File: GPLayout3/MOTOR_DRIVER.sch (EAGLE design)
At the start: 94 parts, among them T1 2N2222, T2 2N2222, U7 ATMEGA328P_TQFP, Y1 16MHz

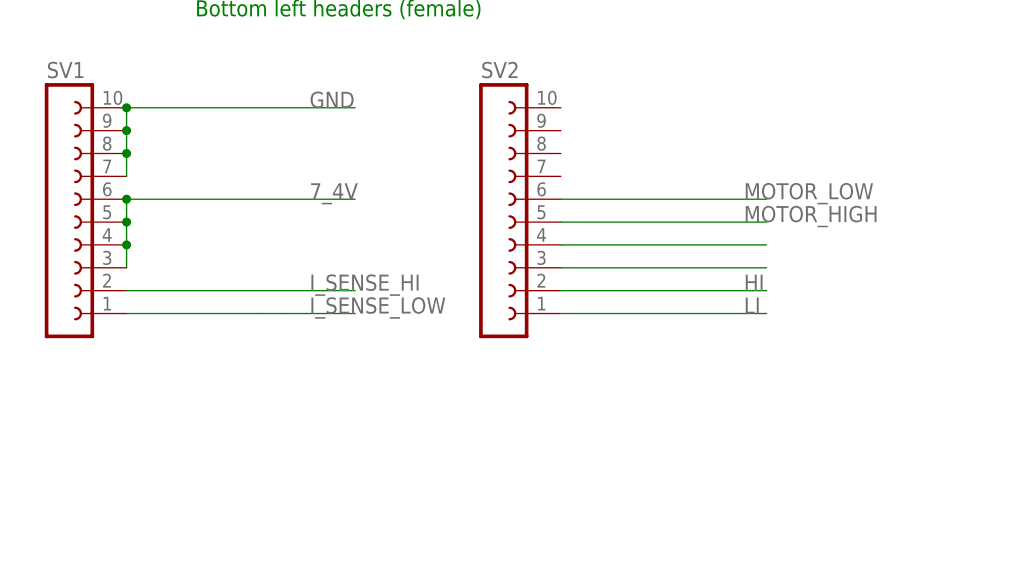
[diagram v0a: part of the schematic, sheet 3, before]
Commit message: Routed lower board and combined all boards
typical_4pcb.dru lists design errors for the width of the traces, but
the file is outdated and trace widths correspond with 4pcb's website
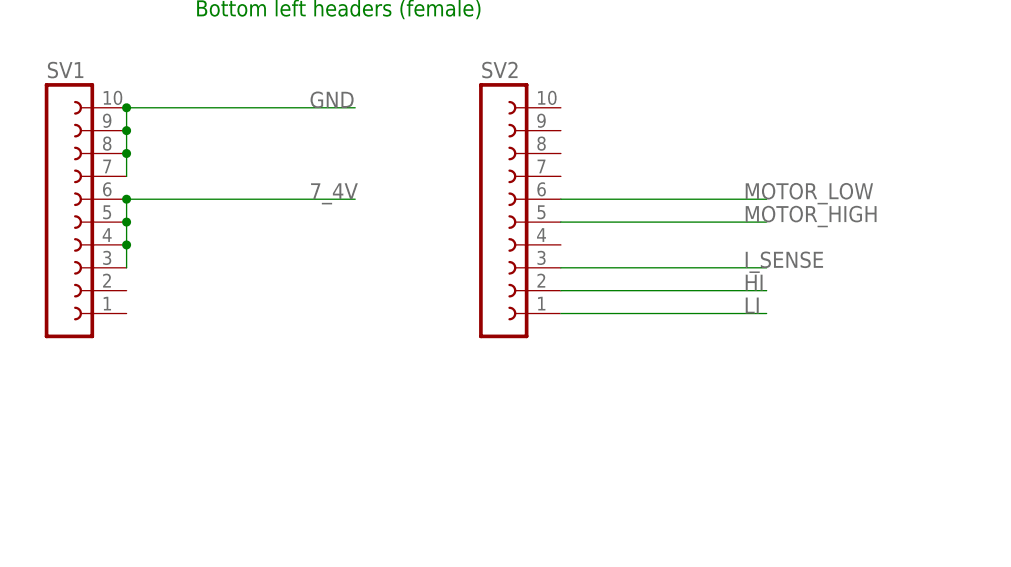
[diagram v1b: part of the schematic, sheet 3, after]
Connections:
- removed net I_SENSE_HI: SV1.2
- removed net I_SENSE_LOW: SV1.1
- net HI2: no longer SV2.3
- net I_SENSE: now also SV2.3
- net LI2: no longer SV2.4
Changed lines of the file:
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@@
 </variantdefs>
 <classes>
-<class number="0" name="default" width="0" drill="0">
-<clearance class="0" value="0.205"/>
+<class number="0" name="default" width="0.2" drill="0.6">
+<clearance class="0" value="0.2"/>
 </class>
 </classes>
@@
 </segment>
 </net>
-<net name="LI2" class="0">
-<segment>
-<pinref part="SV2" gate="G$1" pin="4"/>
-<wire x1="104.14" y1="142.24" x2="127" y2="142.24" width="0.1524" layer="91"/>
-</segment>
-</net>
-<net name="HI2" class="0">
-<segment>
-<pinref part="SV2" gate="G$1" pin="3"/>
-<wire x1="104.14" y1="139.7" x2="127" y2="139.7" width="0.1524" layer="91"/>
-</segment>
-</net>
 <net name="I_SENSE_LOW_TOP" class="0">
 <segment>
@@
 </segment>
 </net>
-<net name="I_SENSE_HI" class="0">
-<segment>
-<pinref part="SV1" gate="G$1" pin="2"/>
-<wire x1="55.88" y1="137.16" x2="81.28" y2="137.16" width="0.1524" layer="91"/>
-<label x="76.2" y="137.16" size="1.778" layer="95"/>
-</segment>
-</net>
-<net name="I_SENSE_LOW" class="0">
-<segment>
-<pinref part="SV1" gate="G$1" pin="1"/>
-<wire x1="55.88" y1="134.62" x2="71.12" y2="134.62" width="0.1524" layer="91"/>
-<wire x1="73.66" y1="134.62" x2="81.28" y2="134.62" width="0.1524" layer="91"/>
-<wire x1="73.66" y1="134.62" x2="71.12" y2="134.62" width="0.1524" layer="91"/>
-<label x="76.2" y="134.62" size="1.778" layer="95"/>
-</segment>
-</net>
 <net name="I_SENSE_TOP" class="0">
 <segment>
@@
 </segment>
 </net>
+<net name="I_SENSE" class="0">
+<segment>
+<pinref part="SV2" gate="G$1" pin="3"/>
+<wire x1="104.14" y1="139.7" x2="127" y2="139.7" width="0.1524" layer="91"/>
+<label x="124.46" y="139.7" size="1.778" layer="95"/>
+</segment>
+</net>

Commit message: added several resistor values
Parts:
- R10, R11, R9: value (none) -> 59
- R5, R7: value (none) -> 1
- renumbered SV10 to TGPIO
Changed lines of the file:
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@@
 <?xml version="1.0" encoding="utf-8"?>
 <!DOCTYPE eagle SYSTEM "eagle.dtd">
-<eagle version="8.0.0">
+<eagle version="8.0.1">
 <drawing>
 <settings>
@@
 <part name="LED_DRIVER2" library="CSD18502KCS" deviceset="CSD18502KCS_KCS_3" device=""/>
 <part name="U$7" library="ledpot" deviceset="POT" device=""/>
-<part name="R5" library="rcl" deviceset="R-US_" device="R2512"/>
+<part name="R5" library="rcl" deviceset="R-US_" device="R2512" value="1"/>
 <part name="T1" library="transistor" deviceset="2N2222" device=""/>
 <part name="R6" library="SparkFun-Resistors" deviceset="1KOHM" device="-HORIZ-1/4W-1%" value="1k"/>
 <part name="LED_DRIVER1" library="CSD18502KCS" deviceset="CSD18502KCS_KCS_3" device=""/>
 <part name="U$3" library="ledpot" deviceset="POT" device=""/>
-<part name="R7" library="rcl" deviceset="R-US_" device="R2512"/>
+<part name="R7" library="rcl" deviceset="R-US_" device="R2512" value="1"/>
 <part name="T2" library="transistor" deviceset="2N2222" device=""/>
 <part name="R8" library="SparkFun-Resistors" deviceset="1KOHM" device="-HORIZ-1/4W-1%" value="1k"/>
@@
 <part name="3_3V" library="con-lsta" deviceset="FE05-1" device=""/>
 <part name="5V" library="con-lsta" deviceset="FE05-1" device=""/>
-<part name="R9" library="rcl" deviceset="R-US_" device="R0805"/>
-<part name="R10" library="rcl" deviceset="R-US_" device="R0805"/>
-<part name="R11" library="rcl" deviceset="R-US_" device="R0805"/>
+<part name="R9" library="rcl" deviceset="R-US_" device="R0805" value="59"/>
+<part name="R10" library="rcl" deviceset="R-US_" device="R0805" value="59"/>
+<part name="R11" library="rcl" deviceset="R-US_" device="R0805" value="59"/>
 <part name="D1" library="SparkFun-LED" deviceset="LED" device="0603"/>
 <part name="D2" library="SparkFun-LED" deviceset="LED" device="0603"/>
@@
 <part name="ATGPIO" library="con-lsta" deviceset="FE10-1" device=""/>
 <part name="R17" library="rcl" deviceset="R-US_" device="R2512" value="10m"/>
-<part name="SV10" library="con-lsta" deviceset="FE08-1" device=""/>
+<part name="TGPIO" library="con-lsta" deviceset="FE08-1" device=""/>
 <part name="I_SENSE_AMP" library="burr-brown" deviceset="INA138" device=""/>
 <part name="R18" library="rcl" deviceset="R-US_" device="R0603" value="10k"/>
@@
 <instance part="R15" gate="G$1" x="360.68" y="86.36" rot="R90"/>
 <instance part="ATGPIO" gate="G$1" x="162.56" y="66.04"/>
-<instance part="SV10" gate="G$1" x="121.92" y="66.04"/>
+<instance part="TGPIO" gate="G$1" x="121.92" y="66.04"/>
 <instance part="REC" gate="G$1" x="208.28" y="91.44"/>
 </instances>
@@
 <wire x1="129.54" y1="58.42" x2="147.32" y2="58.42" width="0.1524" layer="91"/>
 <label x="139.7" y="58.42" size="1.778" layer="95"/>
-<pinref part="SV10" gate="G$1" pin="1"/>
+<pinref part="TGPIO" gate="G$1" pin="1"/>
 </segment>
 </net>
@@
 <wire x1="129.54" y1="60.96" x2="147.32" y2="60.96" width="0.1524" layer="91"/>
 <label x="139.7" y="60.96" size="1.778" layer="95"/>
-<pinref part="SV10" gate="G$1" pin="2"/>
+<pinref part="TGPIO" gate="G$1" pin="2"/>
 </segment>
 </net>
@@
 <wire x1="129.54" y1="63.5" x2="147.32" y2="63.5" width="0.1524" layer="91"/>
 <label x="139.7" y="63.5" size="1.778" layer="95"/>
-<pinref part="SV10" gate="G$1" pin="3"/>
+<pinref part="TGPIO" gate="G$1" pin="3"/>
 </segment>
 </net>
@@
 <wire x1="129.54" y1="66.04" x2="147.32" y2="66.04" width="0.1524" layer="91"/>
 <label x="139.7" y="66.04" size="1.778" layer="95"/>
-<pinref part="SV10" gate="G$1" pin="4"/>
+<pinref part="TGPIO" gate="G$1" pin="4"/>
 </segment>
 </net>
@@
 <wire x1="129.54" y1="68.58" x2="147.32" y2="68.58" width="0.1524" layer="91"/>
 <label x="139.7" y="68.58" size="1.778" layer="95"/>
-<pinref part="SV10" gate="G$1" pin="5"/>
+<pinref part="TGPIO" gate="G$1" pin="5"/>
 </segment>
 </net>
@@
 <wire x1="129.54" y1="71.12" x2="147.32" y2="71.12" width="0.1524" layer="91"/>
 <label x="139.7" y="71.12" size="1.778" layer="95"/>
-<pinref part="SV10" gate="G$1" pin="6"/>
+<pinref part="TGPIO" gate="G$1" pin="6"/>
 </segment>
 </net>
@@
 <wire x1="129.54" y1="73.66" x2="147.32" y2="73.66" width="0.1524" layer="91"/>
 <label x="139.7" y="73.66" size="1.778" layer="95"/>
-<pinref part="SV10" gate="G$1" pin="7"/>
+<pinref part="TGPIO" gate="G$1" pin="7"/>
 </segment>
 </net>
@@
 <wire x1="129.54" y1="76.2" x2="147.32" y2="76.2" width="0.1524" layer="91"/>
 <label x="139.7" y="76.2" size="1.778" layer="95"/>
-<pinref part="SV10" gate="G$1" pin="8"/>
-</segment>
-</net>
+<pinref part="TGPIO" gate="G$1" pin="8"/>
+</segment>
+</net>

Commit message: made overall dimensions smaller, moved I_SENSE and added back a GPIO. made an attempt at a gerber file
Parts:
- removed TGPIO: (no value), con-lsta:FE08-1
- added SV10: (no value), con-lsta:FE09-1
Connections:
- removed net HI2: U$1.5
- new net TGPIO9: SV10.9, U$1.A22/DAC1
- net I_SENSE: now also U$1.5; no longer U$1.A22/DAC1
- net TGPIO1: now also SV10.1; no longer TGPIO.1
- net TGPIO2: now also SV10.2; no longer TGPIO.2
- net TGPIO3: now also SV10.3; no longer TGPIO.3
- net TGPIO4: now also SV10.4; no longer TGPIO.4
- net TGPIO5: now also SV10.5; no longer TGPIO.5
- net TGPIO6: now also SV10.6; no longer TGPIO.6
- net TGPIO7: now also SV10.7; no longer TGPIO.7
- net TGPIO8: now also SV10.8; no longer TGPIO.8
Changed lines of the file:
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@@
 <part name="ATGPIO" library="con-lsta" deviceset="FE10-1" device=""/>
 <part name="R17" library="rcl" deviceset="R-US_" device="R2512" value="10m"/>
-<part name="TGPIO" library="con-lsta" deviceset="FE08-1" device=""/>
 <part name="I_SENSE_AMP" library="burr-brown" deviceset="INA138" device=""/>
 <part name="R18" library="rcl" deviceset="R-US_" device="R0603" value="10k"/>
@@
 <part name="REC" library="con-lsta" deviceset="FE06-1" device=""/>
 <part name="C8" library="rcl" deviceset="C-US" device="C0805" value="10u"/>
+<part name="SV10" library="con-lsta" deviceset="FE09-1" device=""/>
 </parts>
 <sheets>
@@
 </segment>
 </net>
-<net name="HI2" class="0">
-<segment>
-<pinref part="U$1" gate="G$1" pin="5"/>
-<wire x1="238.76" y1="152.4" x2="223.52" y2="152.4" width="0.1524" layer="91"/>
-</segment>
-</net>
 <net name="LI2" class="0">
 <segment>
@@
 <net name="I_SENSE" class="0">
 <segment>
-<pinref part="U$1" gate="G$1" pin="A22/DAC1"/>
-<wire x1="279.4" y1="129.54" x2="294.64" y2="129.54" width="0.1524" layer="91"/>
-<label x="287.02" y="129.54" size="1.778" layer="95"/>
+<pinref part="U$1" gate="G$1" pin="5"/>
+<wire x1="238.76" y1="152.4" x2="223.52" y2="152.4" width="0.1524" layer="91"/>
+<label x="223.52" y="152.4" size="1.778" layer="95"/>
 </segment>
 </net>
@@
 <wire x1="287.02" y1="71.12" x2="269.24" y2="71.12" width="0.1524" layer="91"/>
 <label x="269.24" y="71.12" size="1.778" layer="95"/>
+</segment>
+</net>
+<net name="TGPIO9" class="0">
+<segment>
+<pinref part="U$1" gate="G$1" pin="A22/DAC1"/>
+<wire x1="279.4" y1="129.54" x2="294.64" y2="129.54" width="0.1524" layer="91"/>
+<label x="287.02" y="129.54" size="1.778" layer="95"/>
 </segment>
 </net>
@@
 <instance part="R15" gate="G$1" x="360.68" y="86.36" rot="R90"/>
 <instance part="ATGPIO" gate="G$1" x="162.56" y="66.04"/>
-<instance part="TGPIO" gate="G$1" x="121.92" y="66.04"/>
 <instance part="REC" gate="G$1" x="208.28" y="91.44"/>
+<instance part="SV10" gate="G$1" x="121.92" y="68.58"/>
 </instances>
 <busses>
@@
 <wire x1="129.54" y1="58.42" x2="147.32" y2="58.42" width="0.1524" layer="91"/>
 <label x="139.7" y="58.42" size="1.778" layer="95"/>
-<pinref part="TGPIO" gate="G$1" pin="1"/>
+<pinref part="SV10" gate="G$1" pin="1"/>
 </segment>
 </net>
@@
 <wire x1="129.54" y1="60.96" x2="147.32" y2="60.96" width="0.1524" layer="91"/>
 <label x="139.7" y="60.96" size="1.778" layer="95"/>
-<pinref part="TGPIO" gate="G$1" pin="2"/>
+<pinref part="SV10" gate="G$1" pin="2"/>
 </segment>
 </net>
@@
 <wire x1="129.54" y1="63.5" x2="147.32" y2="63.5" width="0.1524" layer="91"/>
 <label x="139.7" y="63.5" size="1.778" layer="95"/>
-<pinref part="TGPIO" gate="G$1" pin="3"/>
+<pinref part="SV10" gate="G$1" pin="3"/>
 </segment>
 </net>
@@
 <wire x1="129.54" y1="66.04" x2="147.32" y2="66.04" width="0.1524" layer="91"/>
 <label x="139.7" y="66.04" size="1.778" layer="95"/>
-<pinref part="TGPIO" gate="G$1" pin="4"/>
+<pinref part="SV10" gate="G$1" pin="4"/>
 </segment>
 </net>
@@
 <wire x1="129.54" y1="68.58" x2="147.32" y2="68.58" width="0.1524" layer="91"/>
 <label x="139.7" y="68.58" size="1.778" layer="95"/>
-<pinref part="TGPIO" gate="G$1" pin="5"/>
+<pinref part="SV10" gate="G$1" pin="5"/>
 </segment>
 </net>
@@
 <wire x1="129.54" y1="71.12" x2="147.32" y2="71.12" width="0.1524" layer="91"/>
 <label x="139.7" y="71.12" size="1.778" layer="95"/>
-<pinref part="TGPIO" gate="G$1" pin="6"/>
+<pinref part="SV10" gate="G$1" pin="6"/>
 </segment>
 </net>
@@
 <wire x1="129.54" y1="73.66" x2="147.32" y2="73.66" width="0.1524" layer="91"/>
 <label x="139.7" y="73.66" size="1.778" layer="95"/>
-<pinref part="TGPIO" gate="G$1" pin="7"/>
+<pinref part="SV10" gate="G$1" pin="7"/>
 </segment>
 </net>
@@
 <wire x1="129.54" y1="76.2" x2="147.32" y2="76.2" width="0.1524" layer="91"/>
 <label x="139.7" y="76.2" size="1.778" layer="95"/>
-<pinref part="TGPIO" gate="G$1" pin="8"/>
+<pinref part="SV10" gate="G$1" pin="8"/>
 </segment>
 </net>
@@
 </segment>
 </net>
+<net name="TGPIO9" class="0">
+<segment>
+<pinref part="SV10" gate="G$1" pin="9"/>
+<wire x1="129.54" y1="78.74" x2="147.32" y2="78.74" width="0.1524" layer="91"/>
+<label x="139.7" y="78.74" size="1.778" layer="95"/>
+</segment>
+</net>

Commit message: added thermal things for LEDs
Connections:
- new net THERM2: LED2.THERMAL
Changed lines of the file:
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@@
+</segment>
+</net>
+<net name="THERM2" class="0">
+<segment>
+<pinref part="LED2" gate="G$1" pin="THERMAL"/>
+<wire x1="309.88" y1="215.9" x2="307.34" y2="215.9" width="0.1524" layer="91"/>
+<label x="307.34" y="215.9" size="1.778" layer="95"/>
 </segment>
 </net>
